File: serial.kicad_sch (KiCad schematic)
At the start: 9 parts, among them U12 MAX232, U13 W65C51, X2 1.8432MHz

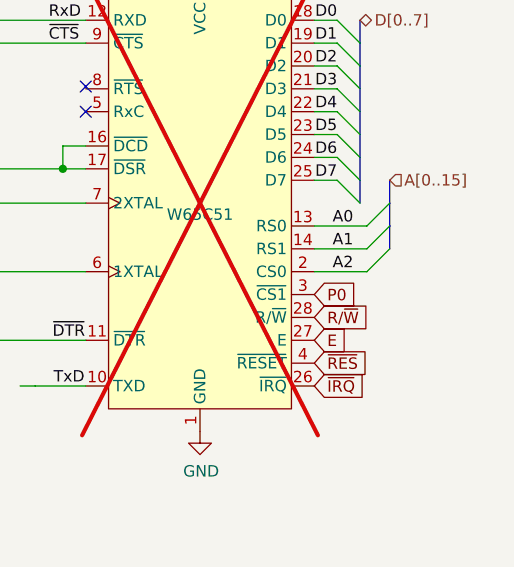
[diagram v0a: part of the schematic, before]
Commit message: complete routing
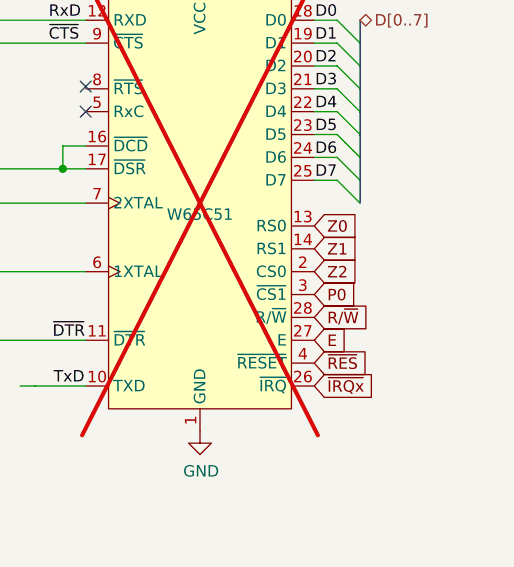
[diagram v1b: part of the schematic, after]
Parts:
- C33, C34, C35, C36: DigiKey (none) -> 732-6416-1-ND
- X2: footprint Crystal:Crystal_SMD_5032-2Pin_5.0x3.2mm_HandSoldering -> Crystal:Crystal_HC49-U_Vertical; DigiKey (none) -> 535-9009-ND
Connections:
- net A0 renamed Z0
- net A1 renamed Z1
- net A2 renamed Z2
- net ~{IRQ} renamed ~{IRQx}

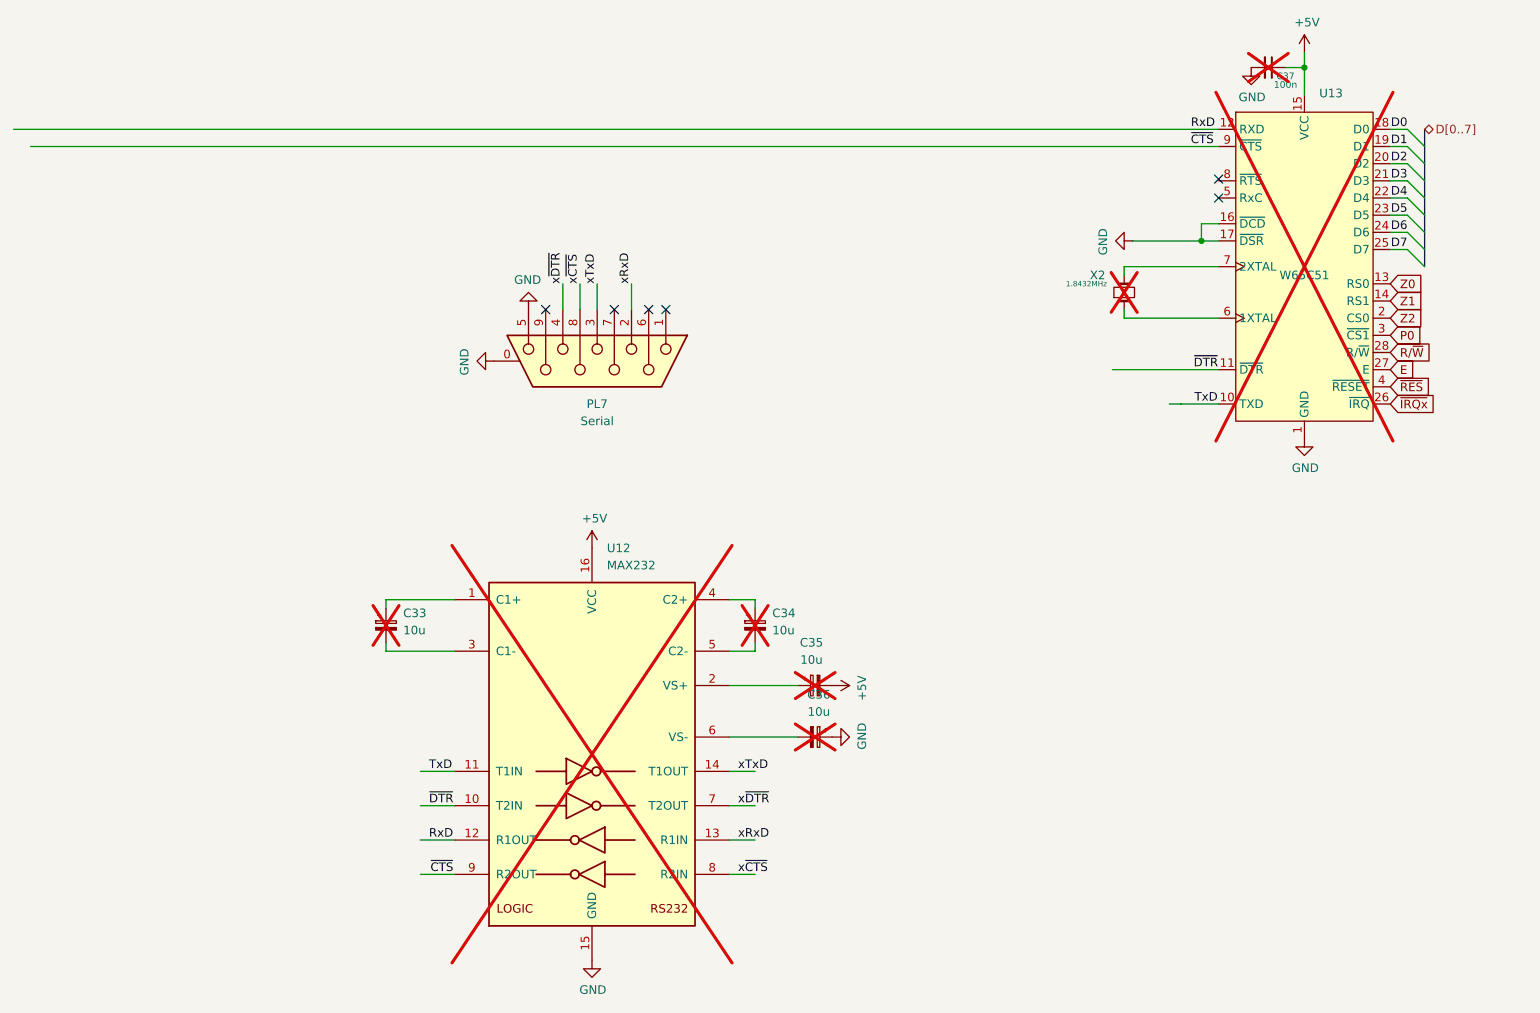
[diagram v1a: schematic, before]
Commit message: route data bus to sam
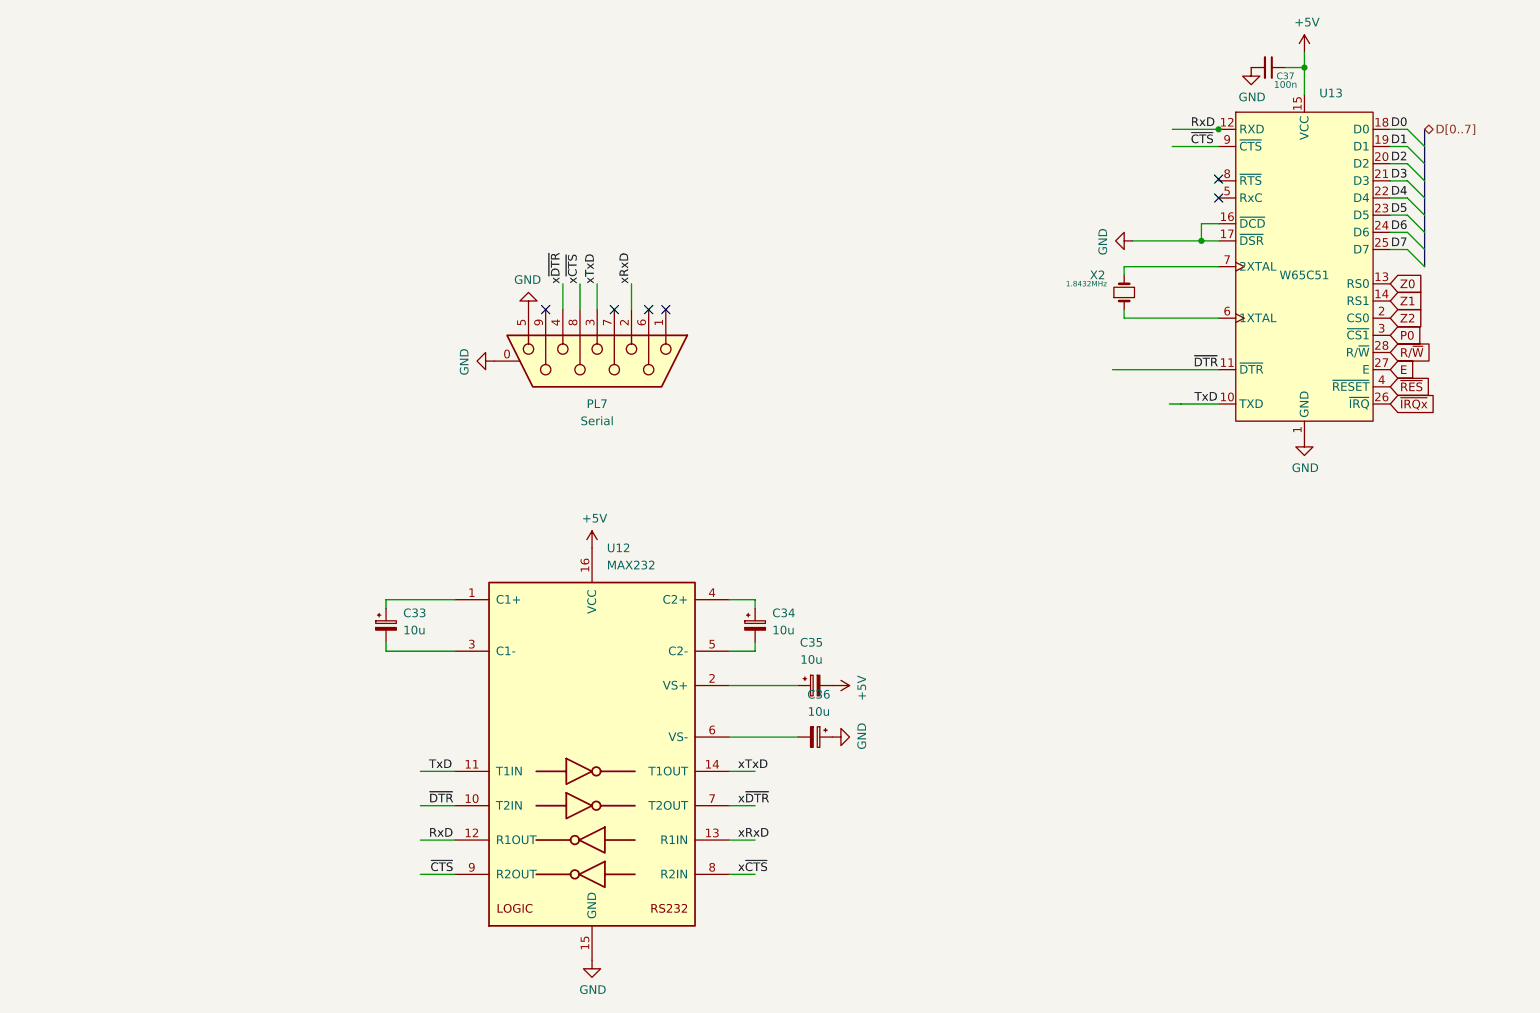
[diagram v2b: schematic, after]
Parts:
- C33, C34, C35, C36, C37, U12, U13, X2: now fitted
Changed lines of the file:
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@@
+	)
+	(junction
+		(at 216.408 40.64)
+		(diameter 0)
+		(color 0 0 0 0)
 	)
 	(junction
@@
 		)
 	)
-	(wire
-		(pts
-			(xy 38.1 40.64) (xy 216.408 40.64)
-		)
-		(stroke
-			(width 0)
-			(type default)
-		)
-	)
 	(bus
 		(pts
@@
 	(wire
 		(pts
+			(xy 209.55 40.64) (xy 216.408 40.64)
+		)
+		(stroke
+			(width 0)
+			(type default)
+		)
+	)
+	(wire
+		(pts
 			(xy 244.348 48.26) (xy 241.808 48.26)
 		)
@@
 	(wire
 		(pts
-			(xy 216.408 43.18) (xy 40.64 43.18)
+			(xy 216.6164 40.64) (xy 216.408 40.64)
+		)
+		(stroke
+			(width 0)
+			(type default)
+		)
+	)
+	(wire
+		(pts
+			(xy 216.408 43.18) (xy 209.55 43.18)
 		)
 		(stroke
@@
 		(in_bom yes)
 		(on_board yes)
-		(dnp yes)
+		(dnp no)
 		(property "Reference" "C37"
 			(at 226.314 32.766 90)
@@
 		(in_bom yes)
 		(on_board yes)
-		(dnp yes)
+		(dnp no)
 		(fields_autoplaced yes)
 		(property "Reference" "C36"
@@
 		(in_bom yes)
 		(on_board yes)
-		(dnp yes)
+		(dnp no)
 		(property "Reference" "C35"
 			(at 156.1719 116.586 90)
@@
 		(in_bom yes)
 		(on_board yes)
-		(dnp yes)
+		(dnp no)
 		(fields_autoplaced yes)
 		(property "Reference" "U12"
@@
 		(in_bom yes)
 		(on_board yes)
-		(dnp yes)
+		(dnp no)
 		(fields_autoplaced yes)
 		(property "Reference" "C33"
@@
 		(in_bom yes)
 		(on_board yes)
-		(dnp yes)
+		(dnp no)
 		(property "Reference" "X2"
 			(at 197.358 62.23 90)
@@
 		(in_bom yes)
 		(on_board yes)
-		(dnp yes)
+		(dnp no)
 		(fields_autoplaced yes)
 		(property "Reference" "U13"
@@
 		(in_bom yes)
 		(on_board yes)
-		(dnp yes)
+		(dnp no)
 		(fields_autoplaced yes)
 		(property "Reference" "C34"

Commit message: update vendor specific BOM fields
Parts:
- U13: DigiKey (none) -> ED90013-ND
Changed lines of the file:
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@@
+			)
+		)
+		(property "DigiKey" "ED90013-ND"
+			(at 229.108 62.23 0)
+			(effects
+				(font
+					(size 1.27 1.27)
+				)
+				(hide yes)
 			)
 		)

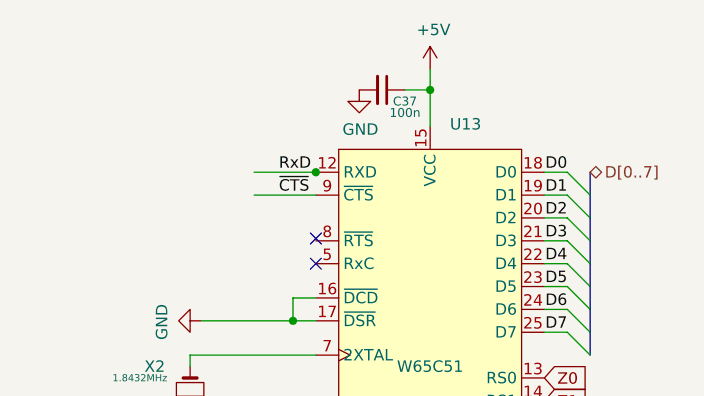
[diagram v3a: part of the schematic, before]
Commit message: add data bus transceiver
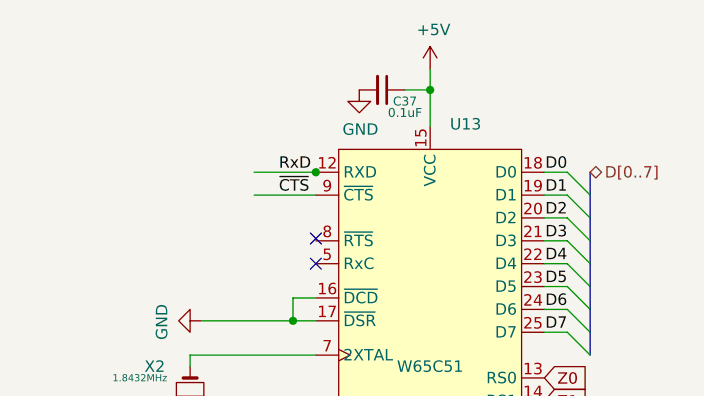
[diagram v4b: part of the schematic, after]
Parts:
- C33, C34, C35, C36: footprint Capacitor_SMD:CP_Elec_5x5.3 -> Capacitor_SMD:CP_Elec_4x5.4; DigiKey 732-6416-1-ND -> 732-8250-1-ND
- C37: value 100n -> 0.1uF; DigiKey (none) -> 399-C0805C104K4RAC7800CT-ND
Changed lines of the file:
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@@
 			)
 		)
-		(property "Value" "100n"
+		(property "Value" "0.1uF"
 			(at 226.314 34.036 90)
 			(effects
@@
 		(property "Description" ""
 			(at 223.774 31.496 0)
+			(effects
+				(font
+					(size 1.27 1.27)
+				)
+				(hide yes)
+			)
+		)
+		(property "DigiKey" "399-C0805C104K4RAC7800CT-ND"
+			(at 223.774 31.496 90)
 			(effects
 				(font
@@
 			)
 		)
-		(property "Footprint" "Capacitor_SMD:CP_Elec_5x5.3"
+		(property "Footprint" "Capacitor_SMD:CP_Elec_4x5.4"
 			(at 156.718 130.556 0)
 			(effects
@@
 			)
 		)
-		(property "DigiKey" "732-6416-1-ND"
+		(property "DigiKey" "732-8250-1-ND"
 			(at 156.718 130.556 90)
 			(effects
@@
 			)
 		)
-		(property "Footprint" "Capacitor_SMD:CP_Elec_5x5.3"
+		(property "Footprint" "Capacitor_SMD:CP_Elec_4x5.4"
 			(at 156.718 122.936 0)
 			(effects
@@
 			)
 		)
-		(property "DigiKey" "732-6416-1-ND"
+		(property "DigiKey" "732-8250-1-ND"
 			(at 156.718 122.936 90)
 			(effects
@@
 			)
 		)
-		(property "Footprint" "Capacitor_SMD:CP_Elec_5x5.3"
+		(property "Footprint" "Capacitor_SMD:CP_Elec_4x5.4"
 			(at 93.218 114.046 0)
 			(effects
@@
 			)
 		)
-		(property "DigiKey" "732-6416-1-ND"
+		(property "DigiKey" "732-8250-1-ND"
 			(at 93.218 114.046 0)
 			(effects
@@
 			)
 		)
-		(property "Footprint" "Capacitor_SMD:CP_Elec_5x5.3"
+		(property "Footprint" "Capacitor_SMD:CP_Elec_4x5.4"
 			(at 147.828 114.046 0)
 			(effects
@@
 			)
 		)
-		(property "DigiKey" "732-6416-1-ND"
+		(property "DigiKey" "732-8250-1-ND"
 			(at 147.828 114.046 0)
 			(effects
